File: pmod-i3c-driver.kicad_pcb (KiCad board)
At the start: 4 copper layers, 75 x 36.5 mm, 80 parts, among them J1 PinSocket_2x12_P2.54mm_Drill1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, J2 PinSocket_2x6_P2.54mm_Drill1.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, J3 JST_SH_1x4_SM04B-SRSS-TB-LF-SN, J4 USB-C_CUI_UJC-HP-3-SMT-TR, J5 PinHeader_1x3_P2.54mm_Drill1.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, J6 PinHeader_1x3_P2.54mm_Drill1.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, J7 PinHeader_2x10_P1.27mm_SMD, Q1 DMC31D5UDJ, Q2 DMC31D5UDJ, Q3 DMC2400UV-7, Q4 DMC2400UV-7, Q5 DMG1012T-7, U1 TPS7A0518P_SOT23-5, U2 SN74LVC1G240_SC70, U3 SN74LVC1G240_SC70, U4 TLV70033_SC70

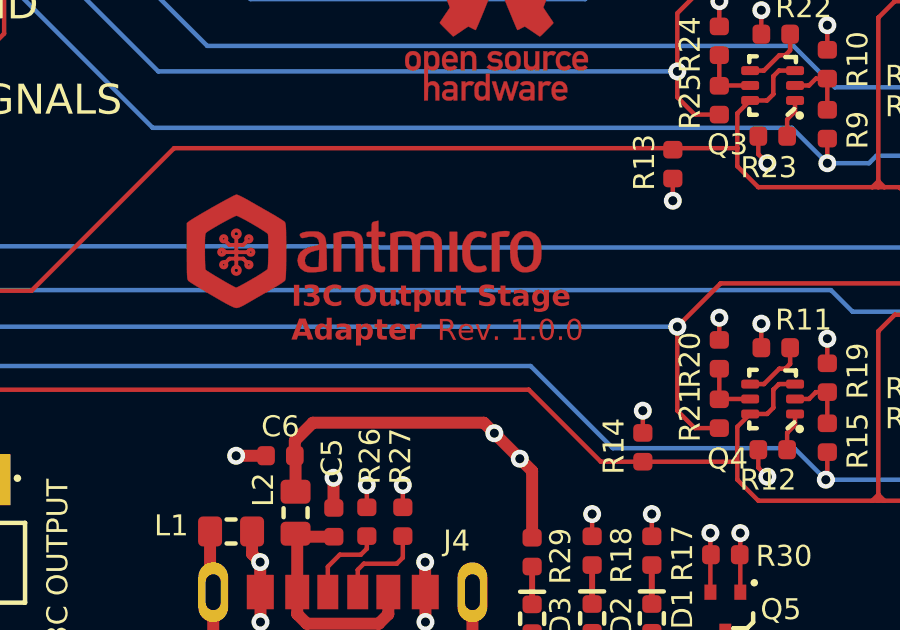
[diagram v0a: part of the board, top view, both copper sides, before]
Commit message: Update naming convention
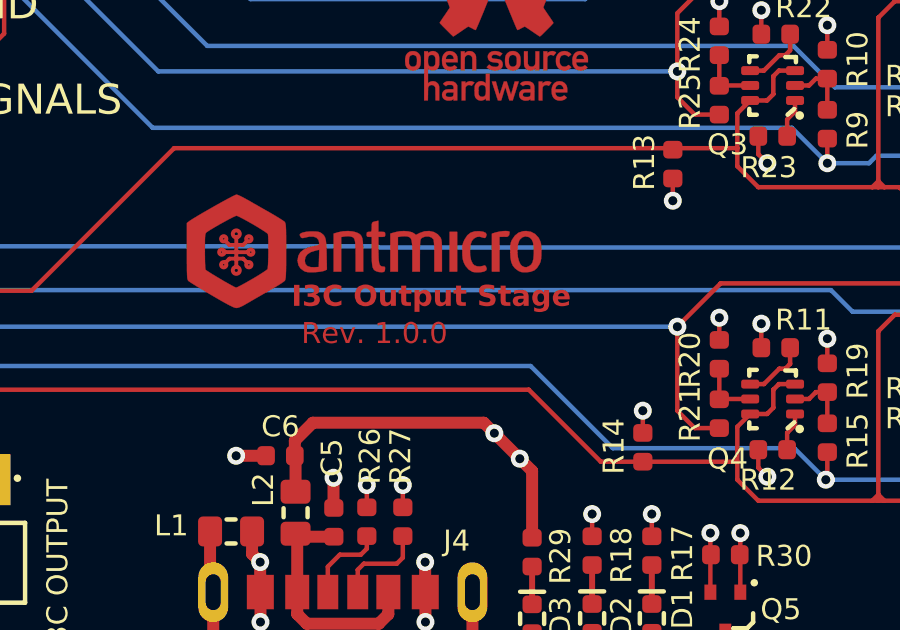
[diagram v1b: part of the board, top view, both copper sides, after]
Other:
- board text added: "I3C Output Stage"
- board text removed: "I3C Output Stage Adapter"

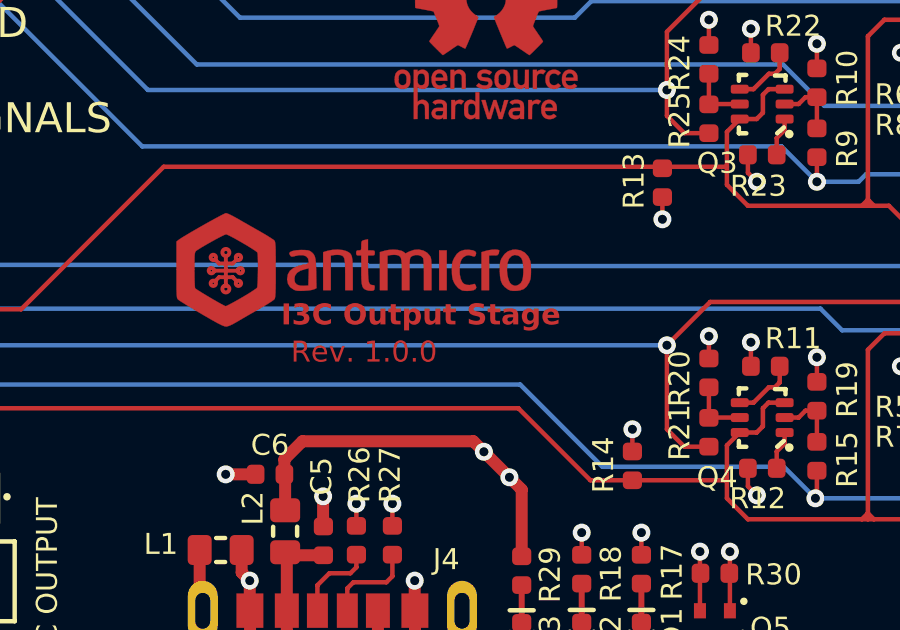
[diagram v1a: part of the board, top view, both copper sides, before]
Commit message: Make J7 DNP
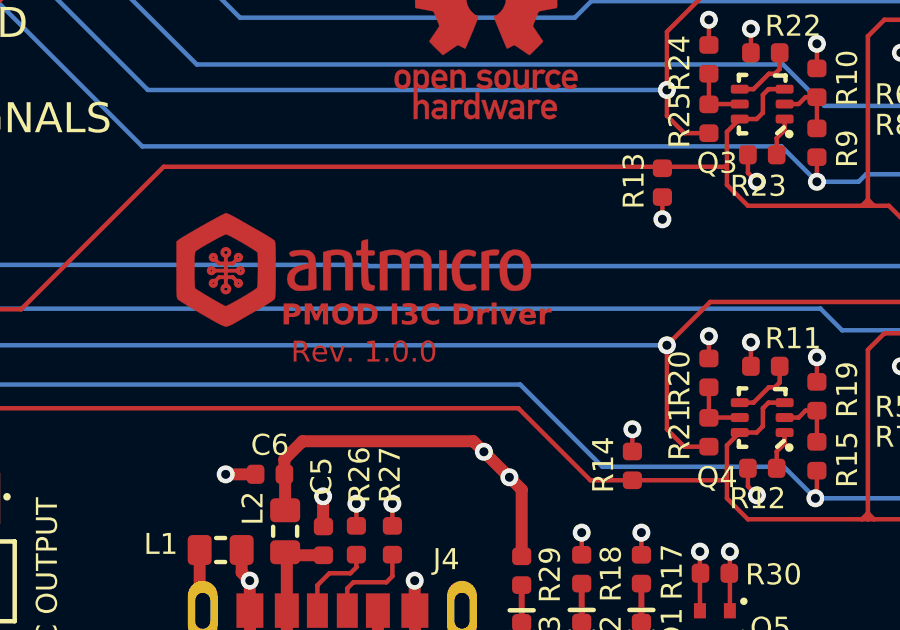
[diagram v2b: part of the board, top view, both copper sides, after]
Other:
- board text added: "PMOD I3C Driver"
- board text removed: "I3C Output Stage"
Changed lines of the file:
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@@
   (gr_line (start 166.7805 99.1935) (end 166.7805 92.6935)
     (stroke (width 0.1) (type default)) (layer "User.5"))
-  (gr_text "I3C Output Stage" (at 154.6765 104.5835) (layer "F.Cu")
+  (gr_text "PMOD I3C Driver" (at 154.6765 104.5835) (layer "F.Cu")
     (effects (font (size 0.7 0.7) (thickness 0.175) bold) (justify left bottom))
   )
@@
     (effects (font (size 0.7 0.7) (thickness 0.15)))
   )
-  (gr_text "I3C Output Stage" (at 154.6765 104.5835) (layer "F.Mask")
+  (gr_text "PMOD I3C Driver" (at 154.6765 104.5835) (layer "F.Mask")
     (effects (font (size 0.7 0.7) (thickness 0.175) bold) (justify left bottom))
   )
